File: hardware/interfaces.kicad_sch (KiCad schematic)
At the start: 0 parts

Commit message: last commit for a while, i have to change the fpga and i dont have the time, money, or motivation to do that
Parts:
- added J?: 472720024, CONN_47272-0024_MOL, symbol arcticvideo:472720024
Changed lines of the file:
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@@
 		(comment 2 "NOT FOR USE IN PRODUCTION")
 	)
+	(symbol
+		(lib_id "arcticvideo:472720024")
+		(at 72.39 45.72 0)
+		(unit 1)
+		(body_style 1)
+		(exclude_from_sim no)
+		(in_bom yes)
+		(on_board yes)
+		(in_pos_files yes)
+		(dnp no)
+		(fields_autoplaced yes)
+		(property "Reference" "J?"
+			(at 86.36 68.5799 0)
+			(show_name no)
+			(do_not_autoplace no)
+			(effects
+				(font
+					(size 1.524 1.524)
+				)
+				(justify left)
+			)
+		)
+		(property "Value" "472720024"
+			(at 86.36 71.1199 0)
+			(show_name no)
+			(do_not_autoplace no)
+			(effects
+				(font
+					(size 1.524 1.524)
+				)
+				(justify left)
+			)
+		)
+		(property "Footprint" "CONN_47272-0024_MOL"
+			(at 72.39 45.72 0)
+			(hide yes)
+			(show_name no)
+			(do_not_autoplace no)
+			(effects
+				(font
+					(size 1.27 1.27)
+					(italic yes)
+				)
+			)
+		)
+		(property "Datasheet" "https://www.molex.com/en-us/products/part-detail-pdf/472720024?display=pdf"
+			(at 72.39 45.72 0)
+			(hide yes)
+			(show_name no)
+			(do_not_autoplace no)
+			(effects
+				(font
+					(size 1.27 1.27)
+					(italic yes)
+				)
+			)
+		)
+		(property "Description" ""
+			(at 72.39 45.72 0)
+			(hide yes)
+			(show_name no)
+			(do_not_autoplace no)
+			(effects
+				(font
+					(size 1.27 1.27)
+				)
+			)
+		)
+		(pin "17"
+		)
+		(pin "9"
+		)
+		(pin "12"
+		)
+		(pin "16"
+		)
+		(pin "2"
+		)
+		(pin "13"
+		)
+		(pin "11"
+		)
+		(pin "14"
+		)
+		(pin "15"
+		)
+		(pin "6"
+		)
+		(pin "3"
+		)
+		(pin "7"
+		)
+		(pin "4"
+		)
+		(pin "8"
+		)
+		(pin "10"
+		)
+		(pin "5"
+		)
+		(pin "1"
+		)
+		(pin "18"
+		)
+		(pin "19"
+		)
+		(pin "20"
+		)
+		(instances
+			(project "arcticvideo"
+				(path "/9e9873e7-449f-4340-a6d8-702e1fa8c41f/f7a4771d-520d-4383-82f3-66eeb57f27f3"
+					(reference "J?")
+					(unit 1)
+				)
+			)
+		)
+	)
 )

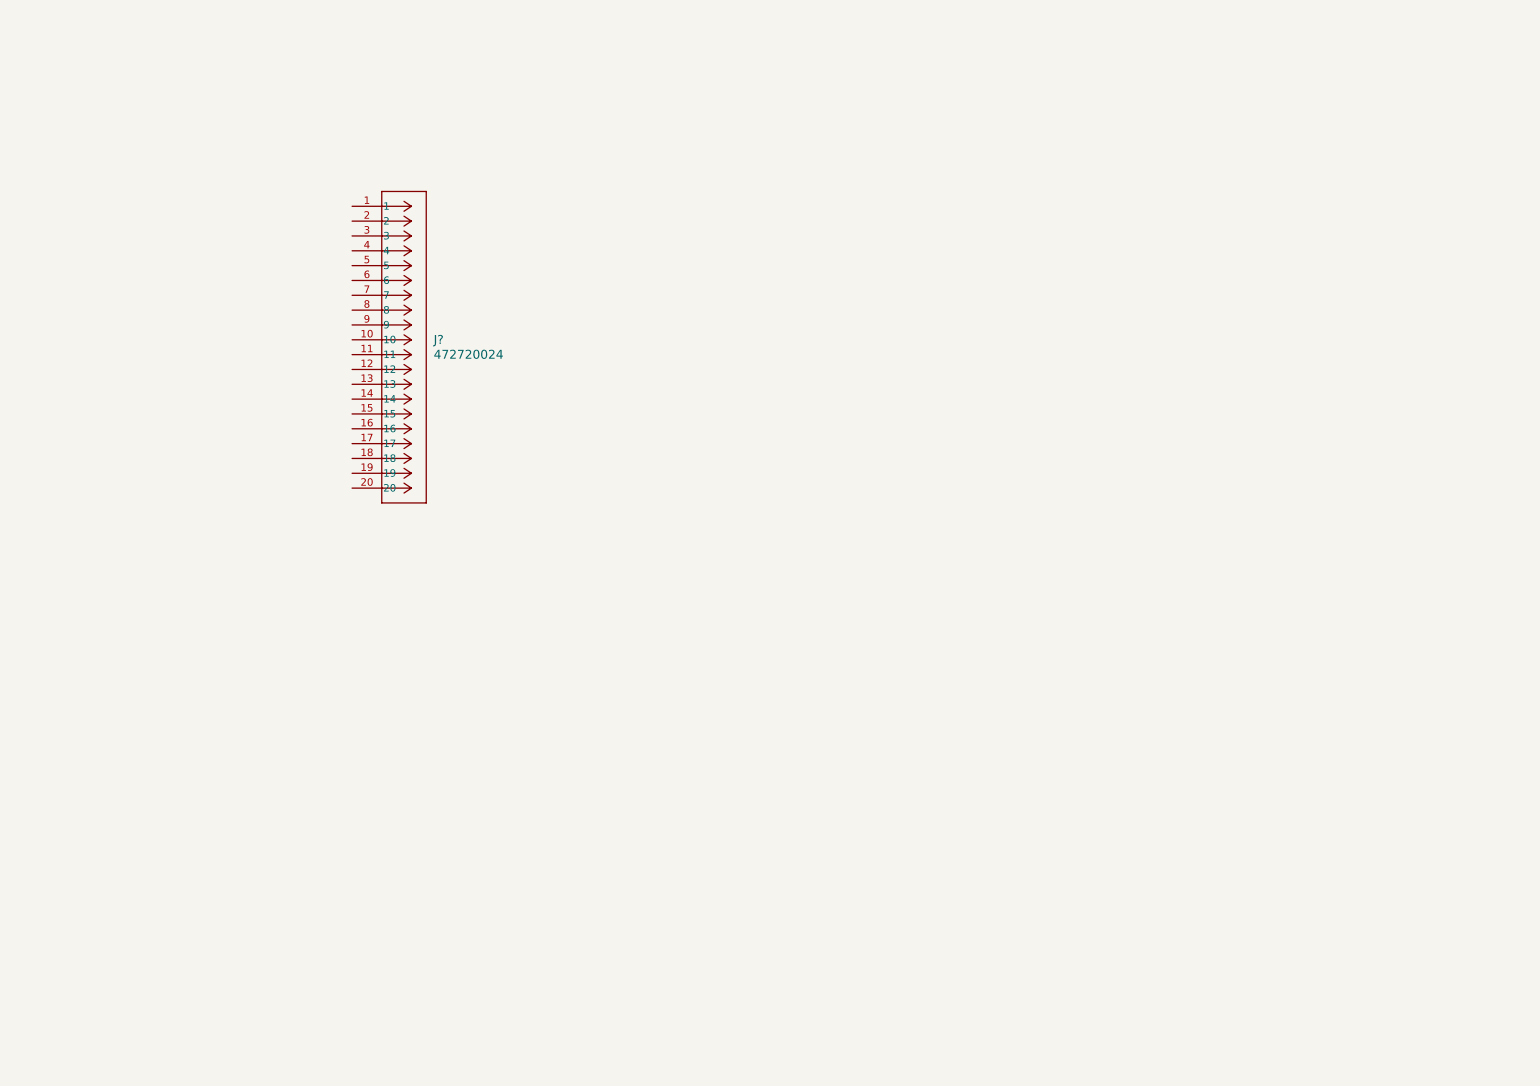
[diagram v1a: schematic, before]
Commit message: finished schematic!!! :D (before peer review)
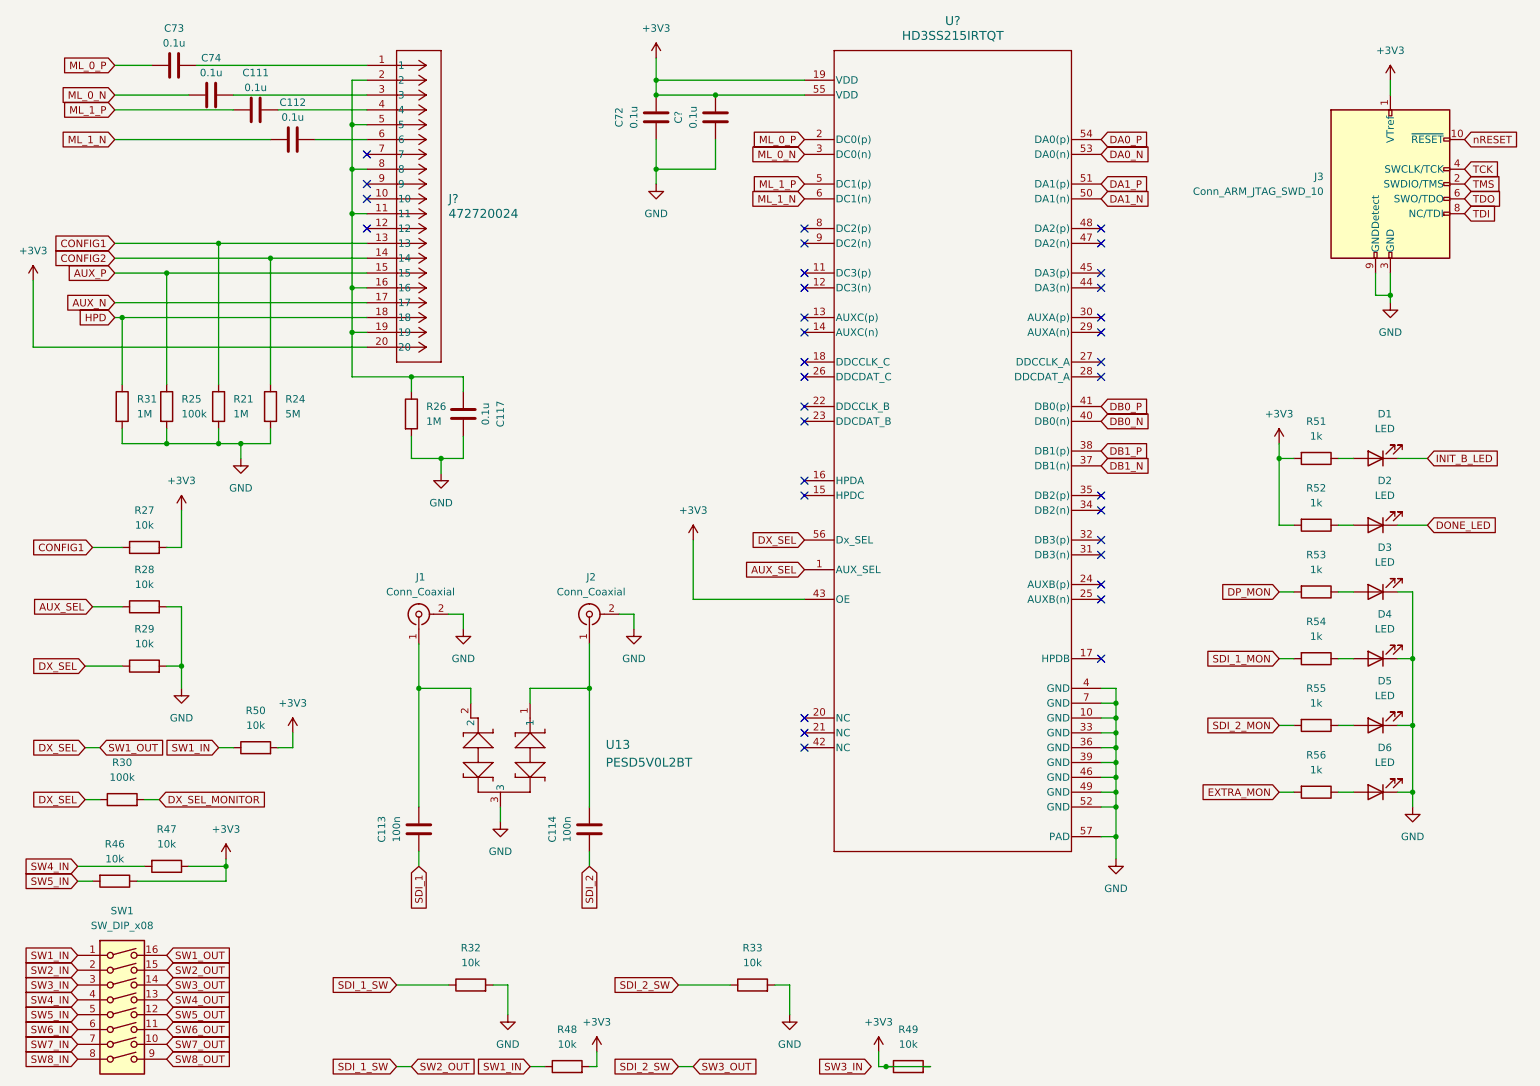
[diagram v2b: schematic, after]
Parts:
- added C111, C112, C117, C72, C73, C74, C?: 0.1u, symbol Device:C
- added C113, C114: 100n, symbol Device:C
- added D1, D2, D3, D4, D5, D6: LED, symbol Device:LED
- added J1, J2: Conn_Coaxial, symbol Connector:Conn_Coaxial
- added J3: Conn_ARM_JTAG_SWD_10, symbol Connector:Conn_ARM_JTAG_SWD_10
- added R21, R26, R31: 1M, symbol Device:R
- added R24: 5M, symbol Device:R
- added R25, R30: 100k, symbol Device:R
- added R27, R28, R29, R32, R33, R46, R47, R48, R49, R50: 10k, symbol Device:R
- added R51, R52, R53, R54, R55, R56: 1k, symbol Device:R
- added SW1: SW_DIP_x08, symbol Switch:SW_DIP_x08
- added U13: PESD5V0L2BT, SOT23_NEX, symbol arcticvideo:PESD5V0L2BT
- added U?: HD3SS215IRTQT, RTQ0056B, symbol arcticvideo:HD3SS215IRTQT
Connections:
- net at J?.1: now also C73.2
- net at J?.11: now also J?.16, J?.19, J?.2, J?.5, J?.8, C117.1, R26.1
- net CONFIG1: now reaches J?.13
- net CONFIG1: now also R21.1, R27.1
- net CONFIG2: now reaches J?.14
- net CONFIG2: now also R24.1
- net AUX_P: now reaches J?.15
- net AUX_P: now also R25.1
- net AUX_N: now reaches J?.17
- net HPD: now reaches J?.18
- net HPD: now also R31.1
- net +3V3: now reaches J?.20
- net +3V3: now also C72.2, C?.2, J3.1 (VTref), R27.2, R46.1, R47.1, R48.2, R49.1, R49.2, R50.2, R51.2, R52.2, U?.19 (VDD), U?.43 (OE), U?.55 (VDD)
- net at J?.3: now also C74.2
- net at J?.4: now also C111.2
- net at J?.6: now also C112.2
- new net: C113.2, J1.1 (In), U13.2
- new net: D1.2 (A), R51.1
- new net: C114.2, J2.1 (In), U13.1
- new net: D2.2 (A), R52.1
- new net: D4.2 (A), R54.1
- new net: D5.2 (A), R55.1
- new net: D6.2 (A), R56.1
- new net: D3.2 (A), R53.1
- new net AUX_SEL: R28.1, U?.1 (AUX_SEL)
- new net DA0_N: U?.53 (DA0(n))
- new net DA0_P: U?.54 (DA0(p))
- new net DA1_N: U?.50 (DA1(n))
- new net DA1_P: U?.51 (DA1(p))
- new net DB0_N: U?.40 (DB0(n))
- new net DB0_P: U?.41 (DB0(p))
- new net DB1_N: U?.37 (DB1(n))
- new net DB1_P: U?.38 (DB1(p))
- new net DONE_LED: D2.1 (K)
- new net DP_MON: R53.2
- new net DX_SEL: R29.1, R30.1, SW1.16, U?.56 (Dx_SEL)
- new net DX_SEL_MONITOR: R30.2
- new net EXTRA_MON: R56.2
- new net GND: C117.2, C72.1, C?.1, D3.1 (K), D4.1 (K), D5.1 (K), D6.1 (K), J1.2 (Ext), J2.2 (Ext), J3.3 (GND), J3.5 (GND), J3.9 (GNDDetect), R21.2, R24.2, R25.2, R26.2, R28.2, R29.2, R31.2, R32.2, R33.2, U13.3, U?.10 (GND), U?.33 (GND), U?.36 (GND), U?.39 (GND), U?.4 (GND), U?.46 (GND), U?.49 (GND), U?.52 (GND), U?.57 (PAD), U?.7 (GND)
- new net INIT_B_LED: D1.1 (K)
- new net ML_0_N: C74.1, U?.3 (DC0(n))
- new net ML_0_P: C73.1, U?.2 (DC0(p))
- new net ML_1_N: C112.1, U?.6 (DC1(n))
- new net ML_1_P: C111.1, U?.5 (DC1(p))
- new net SDI_1: C113.1
- new net SDI_1_MON: R54.2
- new net SDI_1_SW: R32.1, SW1.15
- new net SDI_2: C114.1
- new net SDI_2_MON: R55.2
- new net SDI_2_SW: R33.1, SW1.14
- new net SW1_IN: R48.1, R50.1, SW1.1
- new net SW2_IN: SW1.2
- new net SW3_IN: SW1.3
- new net SW4_IN: R47.2, SW1.4
- new net SW4_OUT: SW1.13
- new net SW5_IN: R46.2, SW1.5
- new net SW5_OUT: SW1.12
- new net SW6_IN: SW1.6
- new net SW6_OUT: SW1.11
- new net SW7_IN: SW1.7
- new net SW7_OUT: SW1.10
- new net SW8_IN: SW1.8
- new net SW8_OUT: SW1.9
- new net TCK: J3.4 (SWCLK/TCK)
- new net TDI: J3.8 (NC/TDI)
- new net TDO: J3.6 (SWO/TDO)
- new net TMS: J3.2 (SWDIO/TMS)
- new net nRESET: J3.10 (~{RESET})
- no-connect marks 0 -> 34
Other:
- moved on the sheet: J?

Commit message: readable changes
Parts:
- removed R49: 10k, symbol Device:R
- added R28: 10k, symbol Device:R
- gave numbers to parts that had none: 3
- renumbered C73 to C88, C74 to C89, C111 to C90, C112 to C91, C113 to C92, C117 to C93, C114 to C94, C72 to C95, J1 to J2, J2 to J3, J3 to J4, R46 to R13, R31 to R14, R30 to R15, R27 to R16, R28 to R17, R29 to R18, R25 to R19, R47 to R20, R50 to R22, R24 to R23, R26 to R24, R32 to R25, R48 to R26, R33 to R27, R51 to R29, R52 to R30, R53 to R31, R54 to R32, R55 to R33, R56 to R34, U13 to U6
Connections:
- net +3V3: now also R28.2
- net SW3_IN: now also R28.1

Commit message: pcb routing
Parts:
- C88, C89, C90, C91, C92, C93, C94, C95, C96: footprint (none) -> Capacitor_SMD:C_0402_1005Metric
- D1, D2, D3, D4, D5, D6: footprint (none) -> LED_SMD:LED_0402_1005Metric
- J1: footprint CONN_47272-0024_MOL -> arcticvideo:CONN_47272-0024_MOL
- J2, J3: footprint (none) -> arcticvideo:SAMTEC_BNC7T-J-P-XX-ST-EM1D
- R11: renamed from R13; footprint (none) -> Resistor_SMD:R_0402_1005Metric
- R12: renamed from R14; footprint (none) -> Resistor_SMD:R_0402_1005Metric
- R13: renamed from R15; footprint (none) -> Resistor_SMD:R_0402_1005Metric
- R14: renamed from R16; footprint (none) -> Resistor_SMD:R_0402_1005Metric
- R15: renamed from R17; footprint (none) -> Resistor_SMD:R_0402_1005Metric
- R16: renamed from R18; footprint (none) -> Resistor_SMD:R_0402_1005Metric
- R17: renamed from R19; footprint (none) -> Resistor_SMD:R_0402_1005Metric
- R18: renamed from R20; footprint (none) -> Resistor_SMD:R_0402_1005Metric
- R19: renamed from R21; footprint (none) -> Resistor_SMD:R_0402_1005Metric
- R20: renamed from R22; footprint (none) -> Resistor_SMD:R_0402_1005Metric
- R21: renamed from R23; footprint (none) -> Resistor_SMD:R_0402_1005Metric
- R22: renamed from R24; footprint (none) -> Resistor_SMD:R_0402_1005Metric
- R23: renamed from R25; footprint (none) -> Resistor_SMD:R_0402_1005Metric
- R24: renamed from R26; footprint (none) -> Resistor_SMD:R_0402_1005Metric
- R25: renamed from R27; footprint (none) -> Resistor_SMD:R_0402_1005Metric
- R26: renamed from R28; footprint (none) -> Resistor_SMD:R_0402_1005Metric
- R27: renamed from R29; footprint (none) -> Resistor_SMD:R_0402_1005Metric
- R28: renamed from R30; footprint (none) -> Resistor_SMD:R_0402_1005Metric
- R29: renamed from R31; footprint (none) -> Resistor_SMD:R_0402_1005Metric
- R30: renamed from R32; footprint (none) -> Resistor_SMD:R_0402_1005Metric
- R31: renamed from R33; footprint (none) -> Resistor_SMD:R_0402_1005Metric
- R32: renamed from R34; footprint (none) -> Resistor_SMD:R_0402_1005Metric
- U6: footprint SOT23_NEX -> arcticvideo:SOT23_NEX
- U7: footprint RTQ0056B -> arcticvideo:RTQ0056B
